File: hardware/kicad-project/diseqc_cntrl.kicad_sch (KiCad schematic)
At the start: 24 parts, among them IC1 TPS560200DBVR, J1 Barrel Jack

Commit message: Corrected 3v3 reg component layout
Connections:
- net +3V3: no longer IC1.5 (VSENSE), R2.2, R3.1
- new net: IC1.5 (VSENSE), R2.2, R3.1
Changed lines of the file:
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@@
-	)
-	(junction
-		(at 111.76 110.49)
-		(diameter 0)
-		(color 0 0 0 0)
 	)
 	(junction
@@
 	)
 	(junction
-		(at 111.76 123.19)
-		(diameter 0)
-		(color 0 0 0 0)
-	)
-	(junction
 		(at 154.94 41.91)
 		(diameter 0)
@@
 	(wire
 		(pts
-			(xy 96.52 110.49) (xy 111.76 110.49)
+			(xy 96.52 110.49) (xy 115.57 110.49)
 		)
 		(stroke
@@
 	(wire
 		(pts
-			(xy 111.76 110.49) (xy 115.57 110.49)
-		)
-		(stroke
-			(width 0)
-			(type default)
-		)
-	)
-	(wire
-		(pts
 			(xy 154.94 41.91) (xy 154.94 39.37)
 		)
@@
 		)
 		(stroke
-			(width 0)
-			(type default)
-		)
-	)
-	(wire
-		(pts
-			(xy 111.76 110.49) (xy 111.76 123.19)
-		)
-		(stroke

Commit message: Removed/rerouted optional component C4
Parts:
- C4: value 1u -> 22pF DNP; now not fitted; now left out of the parts list
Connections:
- net GND: no longer C4.2
- net at IC1.5 (VSENSE), R2.2, R3.1: now also C4.2
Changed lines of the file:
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@@
+	)
+	(junction
+		(at 111.76 123.19)
+		(diameter 0)
+		(color 0 0 0 0)
 	)
 	(junction
@@
 	(wire
 		(pts
-			(xy 125.73 120.65) (xy 125.73 125.73)
+			(xy 125.73 120.65) (xy 125.73 123.19)
 		)
 		(stroke
@@
 		(pts
 			(xy 86.36 121.92) (xy 86.36 120.65)
+		)
+		(stroke
+			(width 0)
+			(type default)
+		)
+	)
+	(wire
+		(pts
+			(xy 111.76 123.19) (xy 125.73 123.19)
 		)
 		(stroke
@@
 	(symbol
 		(lib_id "diseqc_cntrl:GND")
-		(at 125.73 125.73 0)
-		(unit 1)
-		(exclude_from_sim no)
-		(in_bom yes)
-		(on_board yes)
-		(dnp no)
-		(fields_autoplaced yes)
-		(property "Reference" "#PWR09"
-			(at 125.73 132.08 0)
-			(effects
-				(font
-					(size 1.27 1.27)
-				)
-				(hide yes)
-			)
-		)
-		(property "Value" "GND"
-			(at 125.73 130.81 0)
-			(effects
-				(font
-					(size 1.27 1.27)
-				)
-			)
-		)
-		(property "Footprint" ""
-			(at 125.73 125.73 0)
-			(effects
-				(font
-					(size 1.27 1.27)
-				)
-				(hide yes)
-			)
-		)
-		(property "Datasheet" ""
-			(at 125.73 125.73 0)
-			(effects
-				(font
-					(size 1.27 1.27)
-				)
-				(hide yes)
-			)
-		)
-		(property "Description" "Power symbol creates a global label with name \"GND\" , ground"
-			(at 125.73 125.73 0)
-			(effects
-				(font
-					(size 1.27 1.27)
-				)
-				(hide yes)
-			)
-		)
-		(pin "1"
-		)
-		(instances
-			(project "diseqc_cntrl"
-				(path "/82a905d8-f1d7-4995-9c16-94cf3cdcaad9"
-					(reference "#PWR09")
-					(unit 1)
-				)
-			)
-		)
-	)
-	(symbol
-		(lib_id "diseqc_cntrl:GND")
 		(at 186.69 62.23 0)
 		(unit 1)
@@
 		(unit 1)
 		(exclude_from_sim no)
-		(in_bom yes)
+		(in_bom no)
 		(on_board yes)
-		(dnp no)
+		(dnp yes)
 		(fields_autoplaced yes)
 		(property "Reference" "C4"
@@
 			)
 		)
-		(property "Value" "1u"
+		(property "Value" "22pF DNP"
 			(at 129.54 118.1099 0)
 			(effects

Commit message: Starting v0.4 with FT230 fixes; extra TPs
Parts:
- C1, C3: InvenTree Part (none) -> C_10u_0603
- C2: InvenTree Part (none) -> C_2u2_0603
- C5: InvenTree Part (none) -> C_100n_0603; Mouser Part Number 581-KGM15CR51E106MT -> (none)
- C6: InvenTree Part (none) -> C_10u_Electrolytic_25V
- D1: InvenTree Part (none) -> D_Schottky_SS14F
- D2: InvenTree Part (none) -> D_TVS_2A_24V_DO_214AA
- F1: InvenTree Part (none) -> F_Reset_33V_1812
- IC1: InvenTree Part (none) -> VREG_BUCK_4-17VIN_0.8-6.5VOUT_500mA_SOT-23-5
- J1: InvenTree Part (none) -> J_PWR_BARREL_3.9mm
- L1: InvenTree Part (none) -> L_10u_0603
- L2: InvenTree Part (none) -> L_33u_SMD
- PS1: InvenTree Part (none) -> VREG_BUCK_4-36VIN_1-34VOUT_600mA_SOT-23-6
- R1: InvenTree Part (none) -> R_100k_0603
- R2: InvenTree Part (none) -> R_61k9_0603_1%
- R3: InvenTree Part (none) -> R_20k_0603_1%
- R4: InvenTree Part (none) -> R_243k_0603_1%
- R5: InvenTree Part (none) -> R_22k1_0603_1%
- TP1, TP2, TP3, TP4, TP5: now left out of the parts list

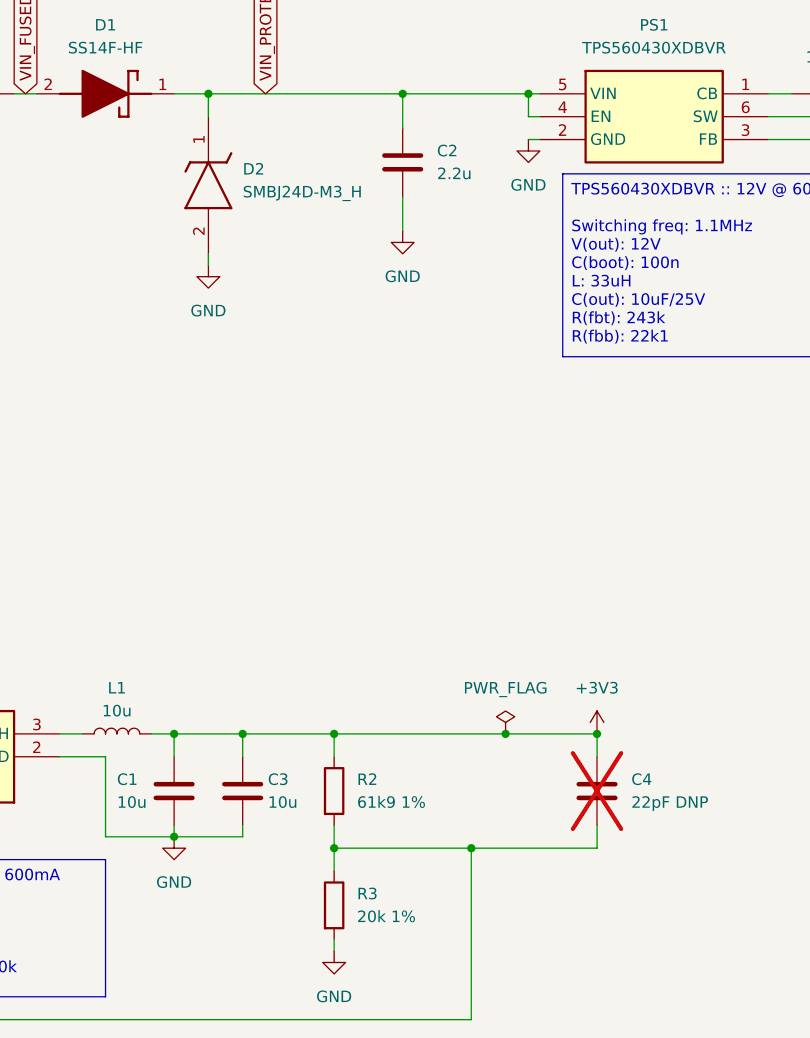
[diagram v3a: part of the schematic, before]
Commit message: Added InvenTree part codes
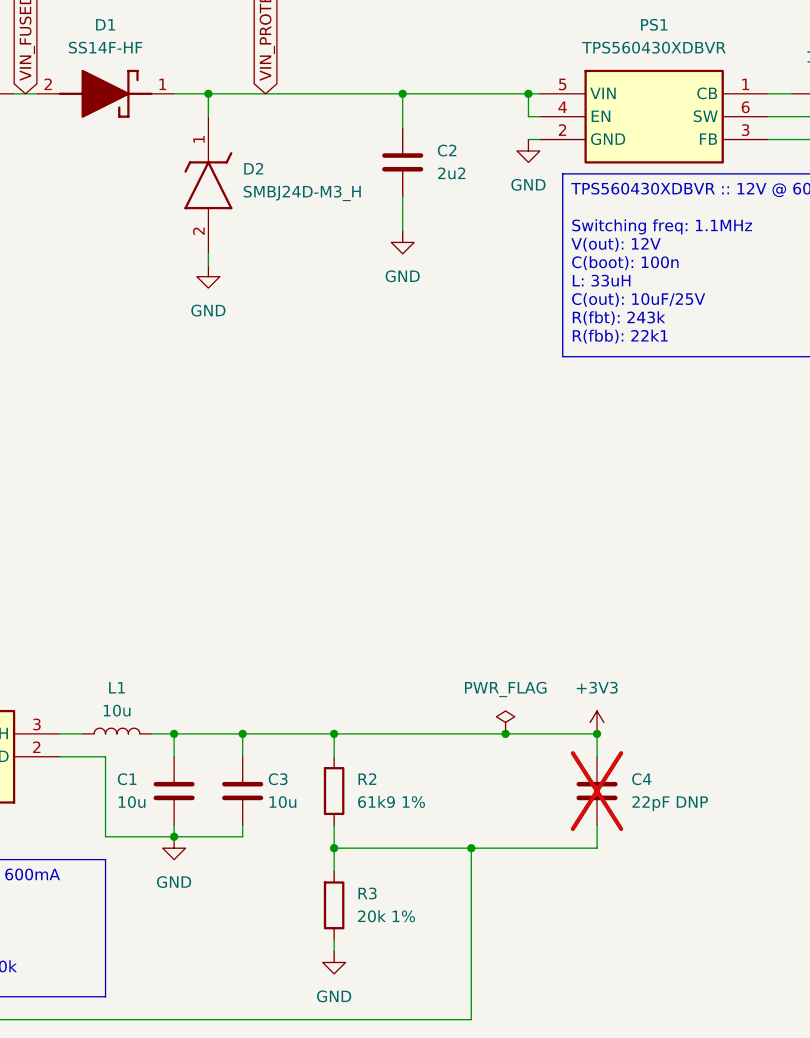
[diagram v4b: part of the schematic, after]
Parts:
- C1: symbol diseqc_cntrl:C -> #InvenTree:C_10u_0603; InvenTree (none) -> 221; Part URL (none) -> https://inventree.ebnx.net/web/part/221/
- C2: value 2.2u -> 2u2; InvenTree (none) -> 71
- C3: InvenTree (none) -> 221
- C5: InvenTree (none) -> 75
- C6: InvenTree (none) -> 90; VoltageRequirement (none) -> >=25V
- D1: InvenTree (none) -> 88
- D2: InvenTree (none) -> 89
- F1: InvenTree (none) -> 94
- IC1: InvenTree (none) -> 125
- J1: InvenTree (none) -> 79
- L1: InvenTree (none) -> 97
- L2: InvenTree (none) -> 95
- PS1: InvenTree (none) -> 127
- R1: InvenTree (none) -> 105
- R2, R3: symbol diseqc_cntrl:R -> #InvenTree:R_61k9_0603; InvenTree (none) -> 222; Part URL (none) -> https://inventree.ebnx.net/web/part/222/; ToleranceRequirement (none) -> <=1%
- R4: InvenTree (none) -> 116; ToleranceRequirement (none) -> <=1%
- R5: InvenTree (none) -> 119; ToleranceRequirement (none) -> <=1%

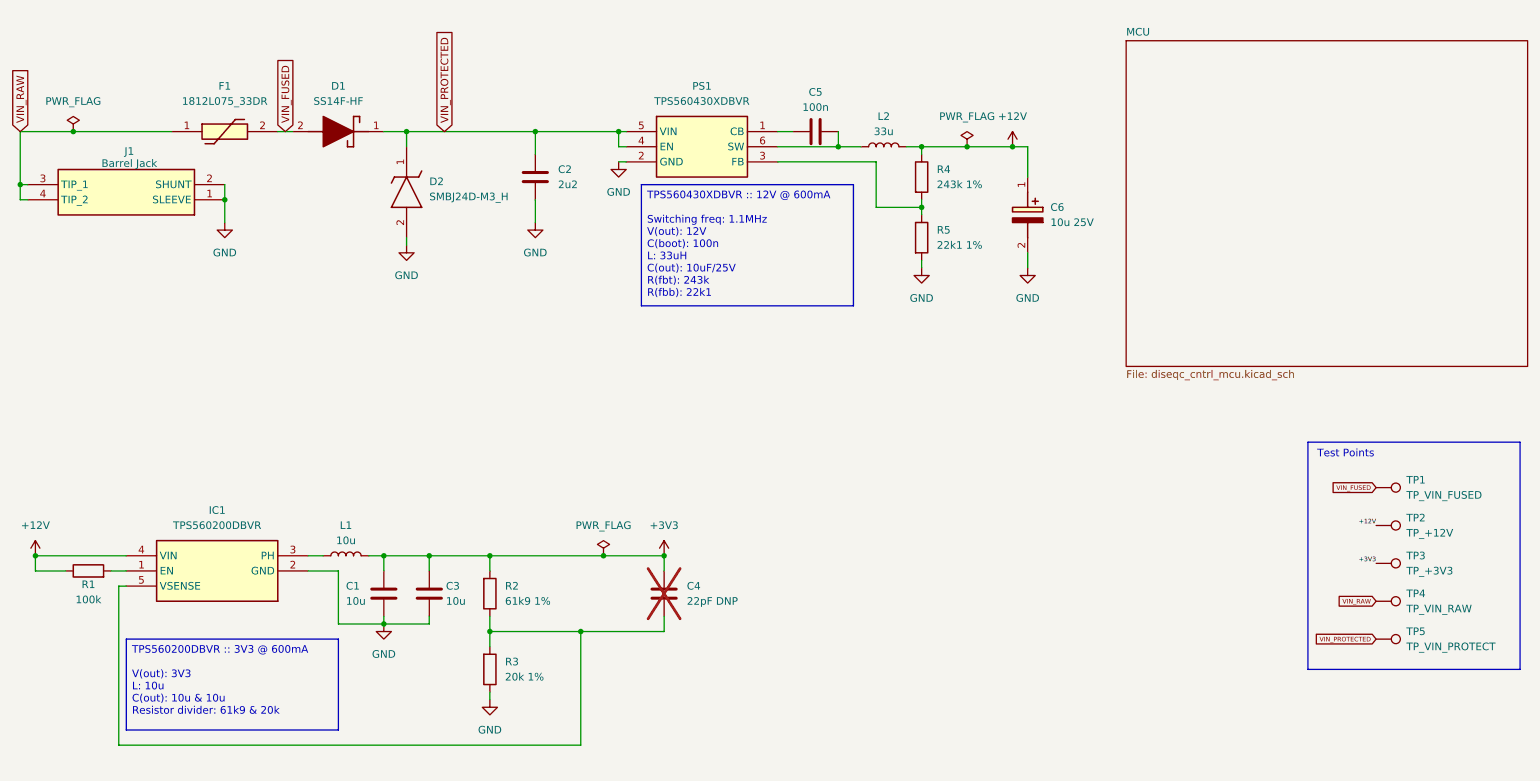
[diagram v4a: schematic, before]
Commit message: nwe board laylout for LAN8742A
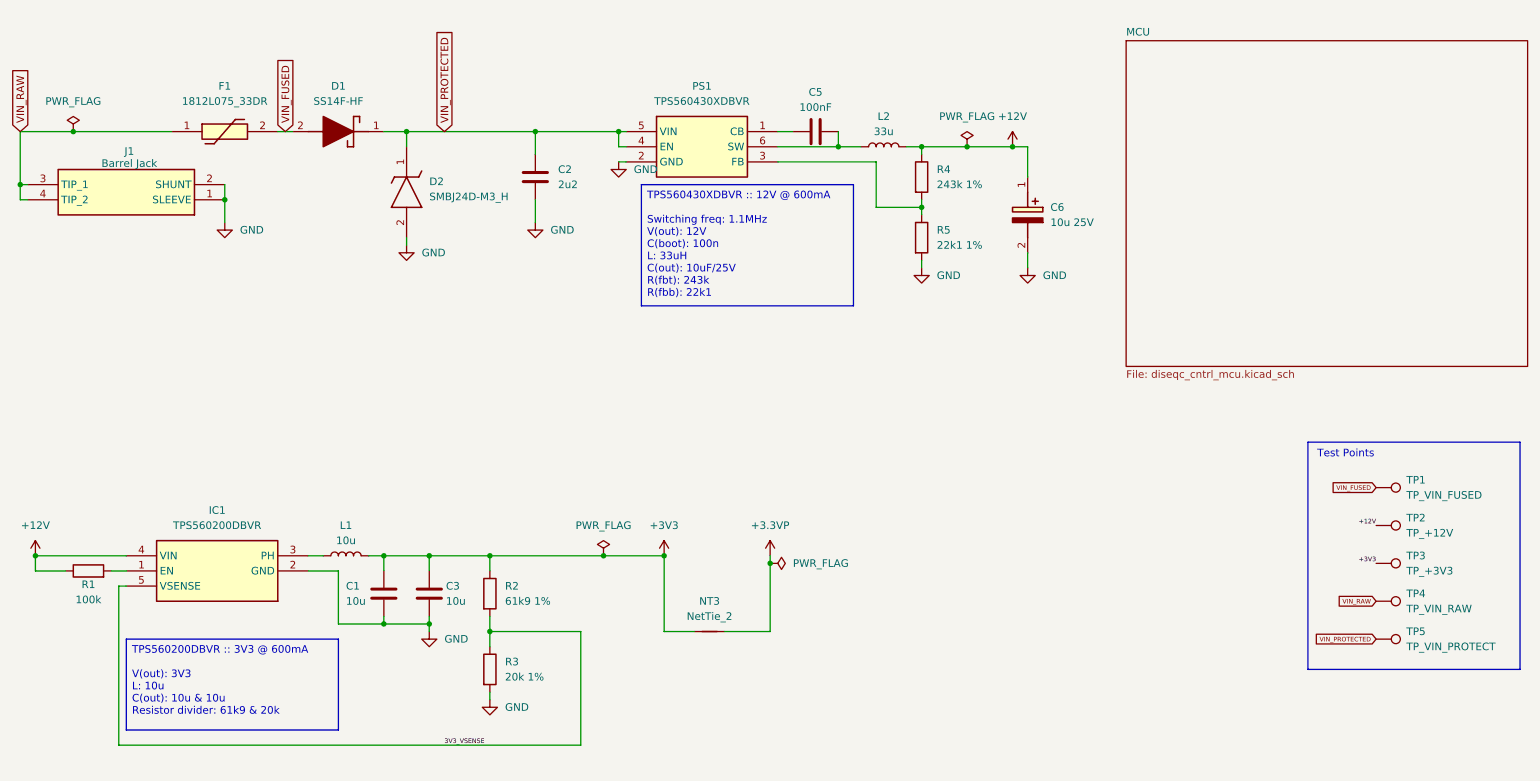
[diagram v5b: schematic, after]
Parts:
- removed C4: 22pF DNP, Capacitor_SMD:C_0603_1608Metric_Pad1.08x0.95mm_HandSolder, symbol diseqc_cntrl:C
- added NT3: NetTie_2, NetTie:NetTie-2_SMD_Pad2.0mm, symbol diseqc_cntrl:NetTie_2
- C5: value 100n -> 100nF
- R2: symbol #InvenTree:R_61k9_0603 -> #InvenTree:R_61k9_0603_1%; InvenTree 222 -> 117; Part URL https://inventree.ebnx.net/web/part/222/ -> https://inventree.ebnx.net/web/part/117/; Tolerance (none) -> 1%
- R3: symbol #InvenTree:R_61k9_0603 -> #InvenTree:R_20k_0603_1%; InvenTree 222 -> 118; Part URL https://inventree.ebnx.net/web/part/222/ -> https://inventree.ebnx.net/web/part/118/; Tolerance (none) -> 1%
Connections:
- net +3V3: now also NT3.1
- net 3V3_VSENSE: now reaches IC1.5 (VSENSE), R2.2, R3.1
- new net +3.3VP: NT3.2

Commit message: Added MCU decoupling
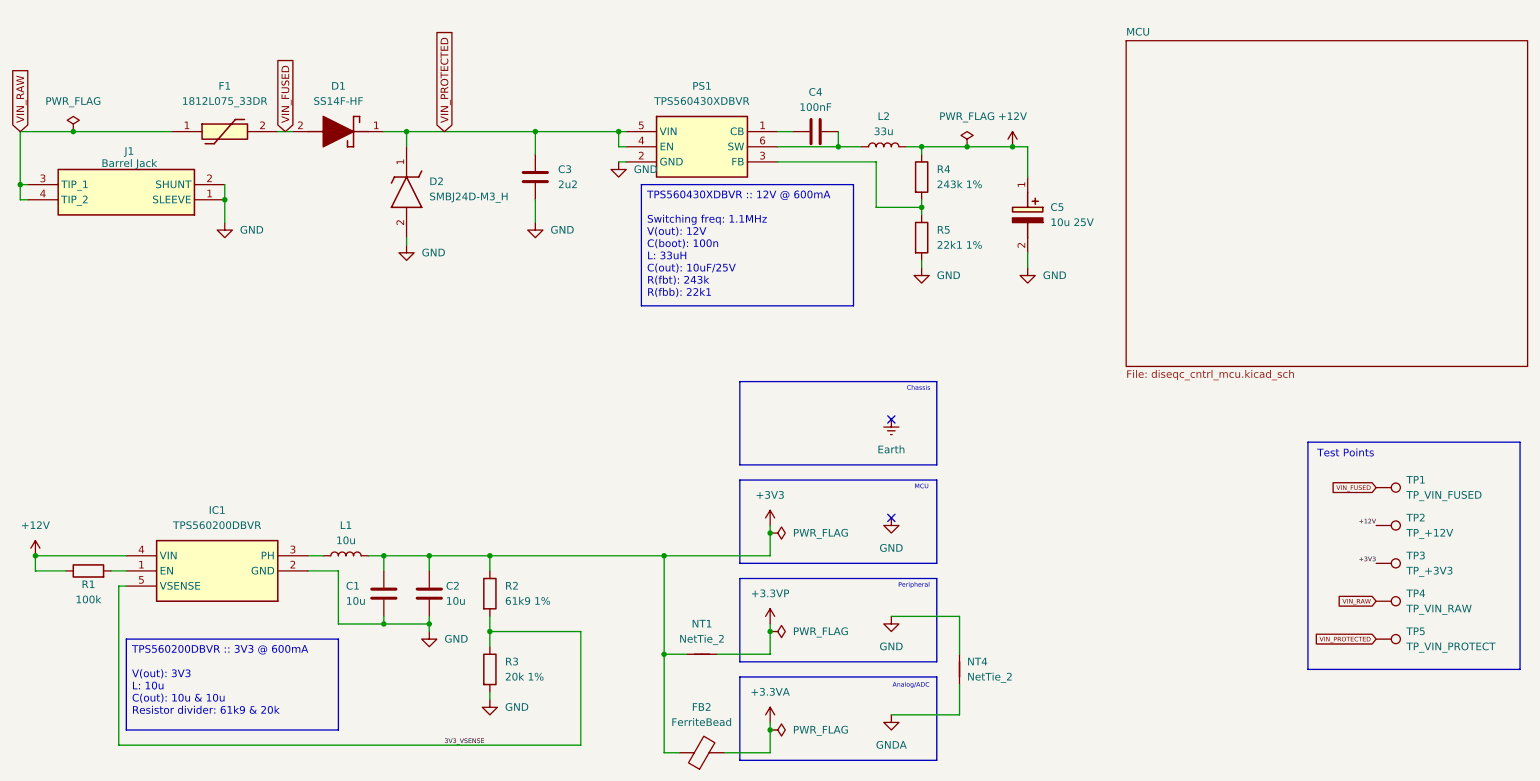
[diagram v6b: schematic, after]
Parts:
- added FB2: FerriteBead, Inductor_SMD:L_0603_1608Metric_Pad1.05x0.95mm_HandSolder, symbol Device:FerriteBead
- added NT4: NetTie_2, NetTie:NetTie-2_SMD_Pad2.0mm, symbol diseqc_cntrl:NetTie_2
- renumbered C3 to C2, C2 to C3, C5 to C4, C6 to C5, NT3 to NT1
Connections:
- net +3V3: now also FB2.1
- net GND: now also NT4.2
- new net +3.3VA: FB2.2
- new net GNDA: NT4.1
- no-connect marks 0 -> 2
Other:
- note added: "Analog/ADC"
- note added: "Chassis"
- note added: "MCU"
- note added: "Peripheral"
- moved on the sheet: NT1

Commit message: Ethernet routing
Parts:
- added TP26: VIN_RAW, TestPoint:TestPoint_Pad_4.0x4.0mm, symbol Connector:TestPoint_Square
- added TP27: GND, TestPoint:TestPoint_Pad_4.0x4.0mm, symbol Connector:TestPoint_Square
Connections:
- net GND: now also TP27.1
- net VIN_RAW: now also TP26.1
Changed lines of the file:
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@@
 	)
 	(junction
+		(at 52.07 57.15)
+		(diameter 0)
+		(color 0 0 0 0)
+	)
+	(junction
 		(at 118.11 39.37)
 		(diameter 0)
@@
 	)
 	(junction
+		(at 17.78 50.8)
+		(diameter 0)
+		(color 0 0 0 0)
+	)
+	(junction
 		(at 78.74 110.49)
 		(diameter 0)
@@
 	(wire
 		(pts
+			(xy 17.78 50.8) (xy 17.78 57.15)
+		)
+		(stroke
+			(width 0)
+			(type default)
+		)
+	)
+	(wire
+		(pts
 			(xy 184.15 41.91) (xy 186.69 41.91)
 		)
@@
 	(wire
 		(pts
+			(xy 43.18 57.15) (xy 52.07 57.15)
+		)
+		(stroke
+			(width 0)
+			(type default)
+		)
+	)
+	(wire
+		(pts
 			(xy 175.26 120.65) (xy 175.26 127)
 		)
@@
 	(wire
 		(pts
-			(xy 52.07 50.8) (xy 52.07 54.61)
+			(xy 52.07 50.8) (xy 52.07 57.15)
 		)
 		(stroke
@@
 	(wire
 		(pts
+			(xy 17.78 48.26) (xy 17.78 50.8)
+		)
+		(stroke
+			(width 0)
+			(type default)
+		)
+	)
+	(wire
+		(pts
 			(xy 78.74 121.92) (xy 86.36 121.92)
 		)
@@
 	(wire
 		(pts
-			(xy 143.51 138.43) (xy 143.51 139.7)
+			(xy 52.07 57.15) (xy 52.07 59.69)
 		)
 		(stroke
@@
 	(wire
 		(pts
-			(xy 154.94 41.91) (xy 154.94 39.37)
+			(xy 143.51 138.43) (xy 143.51 139.7)
 		)
 		(stroke
@@
 	(wire
 		(pts
-			(xy 17.78 50.8) (xy 17.78 48.26)
+			(xy 154.94 41.91) (xy 154.94 39.37)
 		)
 		(stroke
@@
 	)
 	(symbol
+		(lib_id "Connector:TestPoint_Square")
+		(at 17.78 57.15 0)
+		(unit 1)
+		(body_style 1)
+		(exclude_from_sim no)
+		(in_bom yes)
+		(on_board yes)
+		(in_pos_files yes)
+		(dnp no)
+		(fields_autoplaced yes)
+		(property "Reference" "TP26"
+			(at 20.32 55.8799 0)
+			(show_name no)
+			(do_not_autoplace no)
+			(effects
+				(font
+					(size 1.27 1.27)
+				)
+				(justify left)
+			)
+		)
+		(property "Value" "VIN_RAW"
+			(at 20.32 58.4199 0)
+			(show_name no)
+			(do_not_autoplace no)
+			(effects
+				(font
+					(size 1.27 1.27)
+				)
+				(justify left)
+			)
+		)
+		(property "Footprint" "TestPoint:TestPoint_Pad_4.0x4.0mm"
+			(at 22.86 57.15 0)
+			(hide yes)
+			(show_name no)
+			(do_not_autoplace no)
+			(effects
+				(font
+					(size 1.27 1.27)
+				)
+			)
+		)
+		(property "Datasheet" "~"
+			(at 22.86 57.15 0)
+			(hide yes)
+			(show_name no)
+			(do_not_autoplace no)
+			(effects
+				(font
+					(size 1.27 1.27)
+				)
+			)
+		)
+		(property "Description" "test point"
+			(at 17.78 57.15 0)
+			(hide yes)
+			(show_name no)
+			(do_not_autoplace no)
+			(effects
+				(font
+					(size 1.27 1.27)
+				)
+			)
+		)
+		(pin "1"
+		)
+		(instances
+			(project "diseqc_cntrl"
+				(path "/82a905d8-f1d7-4995-9c16-94cf3cdcaad9"
+					(reference "TP26")
+					(unit 1)
+				)
+			)
+		)
+	)
+	(symbol
 		(lib_id "diseqc_cntrl:PWR_FLAG")
 		(at 143.51 106.68 270)
@@
 	)
 	(symbol
+		(lib_id "Connector:TestPoint_Square")
+		(at 43.18 57.15 0)
+		(unit 1)
+		(body_style 1)
+		(exclude_from_sim no)
+		(in_bom yes)
+		(on_board yes)
+		(in_pos_files yes)
+		(dnp no)
+		(property "Reference" "TP27"
+			(at 37.338 55.88 0)
+			(show_name no)
+			(do_not_autoplace no)
+			(effects
+				(font
+					(size 1.27 1.27)
+				)
+				(justify left)
+			)
+		)
+		(property "Value" "GND"
+			(at 37.338 58.42 0)
+			(show_name no)
+			(do_not_autoplace no)
+			(effects
+				(font
+					(size 1.27 1.27)
+				)
+				(justify left)
+			)
+		)
+		(property "Footprint" "TestPoint:TestPoint_Pad_4.0x4.0mm"
+			(at 48.26 57.15 0)
+			(hide yes)
+			(show_name no)
+			(do_not_autoplace no)
+			(effects
+				(font
+					(size 1.27 1.27)
+				)
+			)
+		)
+		(property "Datasheet" "~"
+			(at 48.26 57.15 0)
+			(hide yes)
+			(show_name no)
+			(do_not_autoplace no)
+			(effects
+				(font
+					(size 1.27 1.27)
+				)
+			)
+		)
+		(property "Description" "test point"
+			(at 43.18 57.15 0)
+			(hide yes)
+			(show_name no)
+			(do_not_autoplace no)
+			(effects
+				(font
+					(size 1.27 1.27)
+				)
+			)
+		)
+		(pin "1"
+		)
+		(instances
+			(project "diseqc_cntrl"
+				(path "/82a905d8-f1d7-4995-9c16-94cf3cdcaad9"
+					(reference "TP27")
+					(unit 1)
+				)
+			)
+		)
+	)
+	(symbol
 		(lib_id "diseqc_cntrl:SMBJ24D-M3_H")
 		(at 82.55 41.91 270)
@@
 	(symbol
 		(lib_id "power:GND")
-		(at 52.07 54.61 0)
+		(at 52.07 59.69 0)
 		(unit 1)
 		(body_style 1)
@@
 		(fields_autoplaced yes)
 		(property "Reference" "#PWR02"
-			(at 52.07 60.96 0)
+			(at 52.07 66.04 0)
 			(hide yes)
 			(show_name no)
@@
 		)
 		(property "Value" "GND"
-			(at 54.61 55.8799 0)
+			(at 54.61 60.9599 0)
 			(show_name no)
 			(do_not_autoplace no)
@@
 		)
 		(property "Footprint" ""
-			(at 52.07 54.61 0)
+			(at 52.07 59.69 0)
 			(hide yes)
 			(show_name no)
@@
 		)
 		(property "Datasheet" ""
-			(at 52.07 54.61 0)
+			(at 52.07 59.69 0)
 			(hide yes)
 			(show_name no)
@@
 		)
 		(property "Description" "Power symbol creates a global label with name \"GND\" , ground"
-			(at 52.07 54.61 0)
+			(at 52.07 59.69 0)
 			(hide yes)
 			(show_name no)
